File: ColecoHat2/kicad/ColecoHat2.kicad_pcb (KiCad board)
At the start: 2 copper layers, 56 x 65 mm, 20 parts, among them J1 CTRL1, J2 CTRL2, J3 PI_HEADER, J4 CONN_01X06, SW1 BOOTLOADER, SW2 RESET, U1 STM32L011G4U6

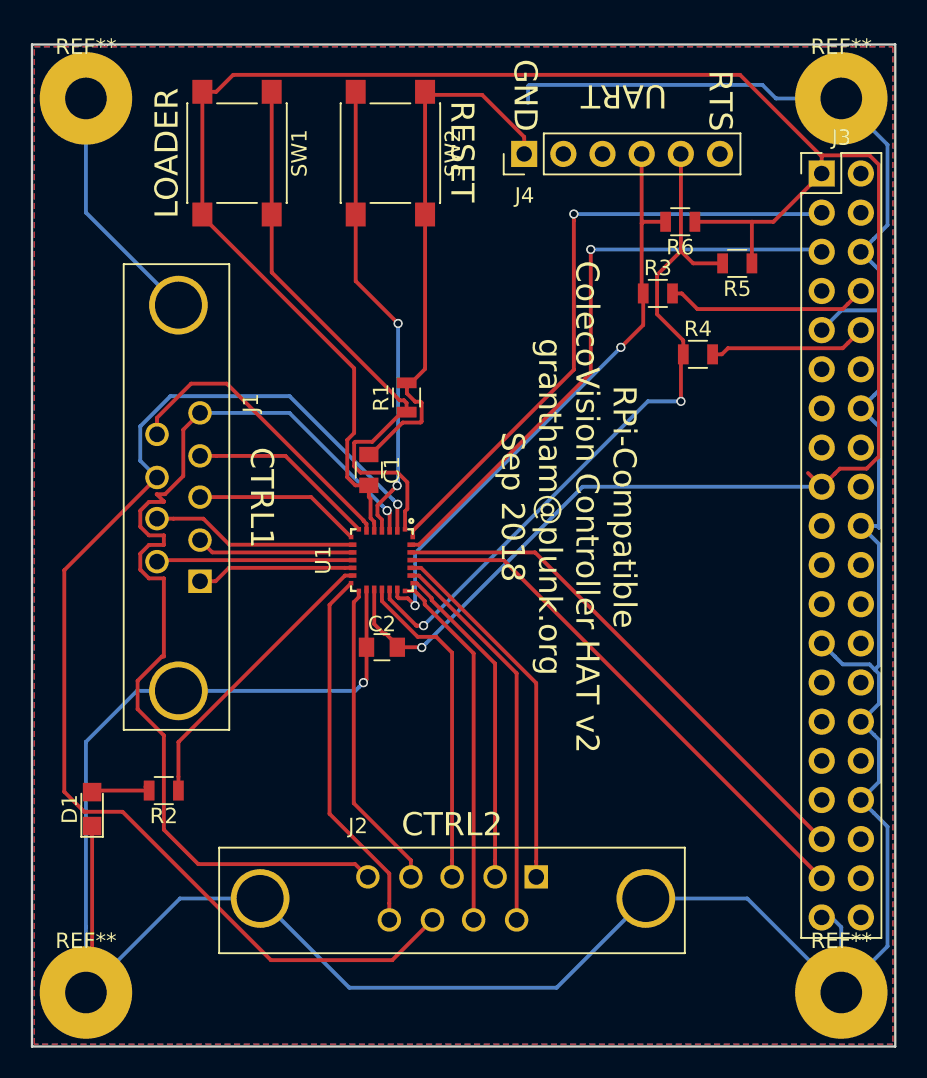
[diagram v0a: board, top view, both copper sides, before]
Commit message: add larger STM32L041K6U6 component
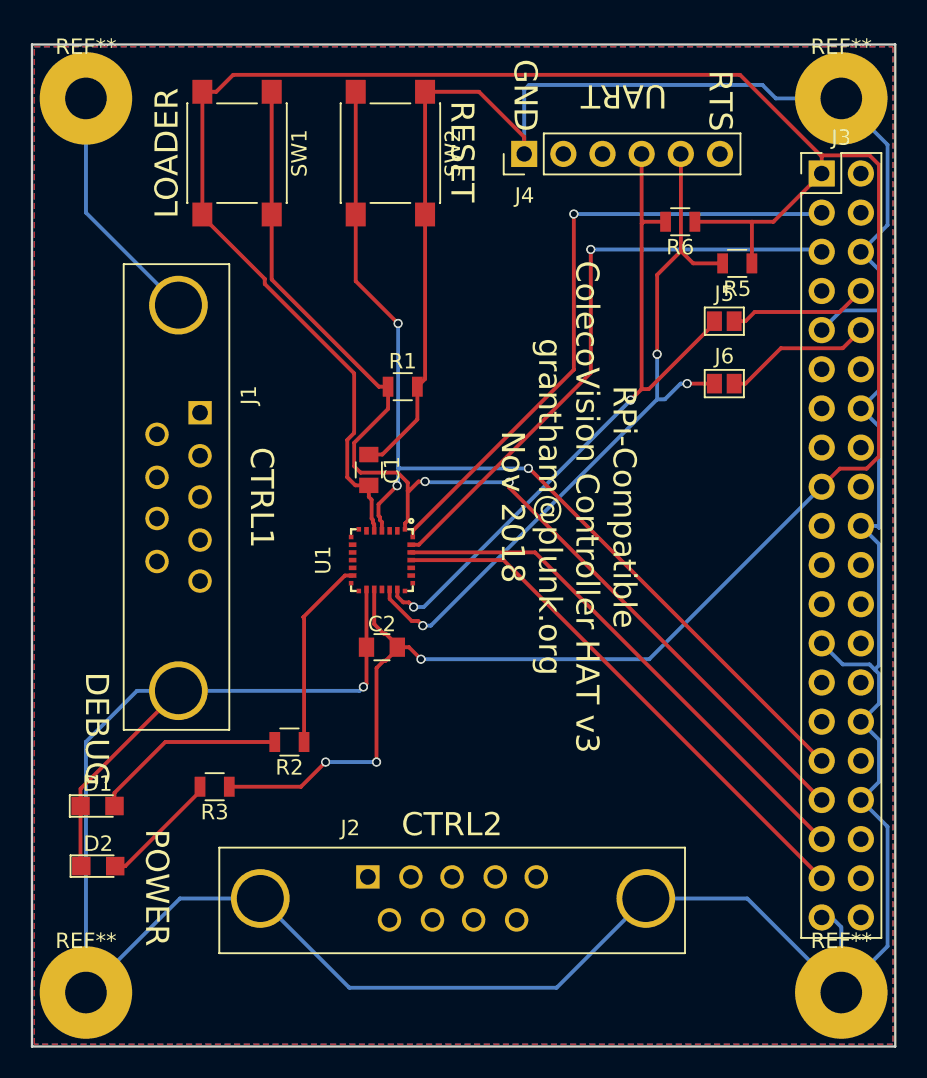
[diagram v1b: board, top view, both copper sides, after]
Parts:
- removed R4: 0, Resistors_SMD:R_0805
- added D2: POWER, LEDs:LED_0805, F.Cu at (131.8, 109.8)
- added J5: GS2, Connectors:GS2, F.Cu at (172.4, 74.5)
- added J6: GS2, Connectors:GS2, F.Cu at (172.4, 78.5)
- D1: value DEBUG LED -> DEBUG
- J1, J2: footprint Connectors:DB9FD -> Connectors:DB9MD
- R2: value 220 -> 470
- R3: value 0 -> 1K
- moved R3 43.0 mm to (139.3, 104.7), turned to 180 degrees
- moved J1 10.9 mm to (138.4, 80.4)
- moved J2 10.9 mm to (149.3, 110.5)
- moved R2 8.74 mm to (144.2, 101.8)
- moved R1 0.74 mm to (151.6, 78.7), turned to 0 degrees
- moved D1 0.40 mm to (131.8, 105.9), turned to 0 degrees
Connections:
- J3 pad 31: Net-(J3-Pad31) -> NRST
- J3 pad 33: Net-(J3-Pad33) -> BOOTLOADER
- R3 pad 1: USART1_RX -> +3V3
- R3 pad 2: Net-(J3-Pad8) -> Net-(D2-Pad2)
- SW2 pad 2: Net-(SW2-Pad2) -> NRST
- U1 pad 10: S1 -> W1
- U1 pad 11: FIRE1 -> E1
- U1 pad 12: N1 -> QUADB1
- U1 pad 14: QUADB2 -> N2
- U1 pad 15: E2 -> FIRE2
- U1 pad 18: W2 -> S2
- U1 pad 22: S2 -> W2
- U1 pad 23: FIRE2 -> E2
- U1 pad 24: N2 -> QUADB2
- U1 pad 4: Net-(SW2-Pad2) -> NRST
- U1 pad 6: QUADB1 -> N1
- U1 pad 7: E1 -> FIRE1
- U1 pad 8: W1 -> S1
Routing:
- net SELECT_JOYSTICK: track 78.3 -> 0.00 mm, vias 1 -> 0
- net SELECT_KEYPAD: track 65.6 -> 0.00 mm, vias 1 -> 0
- net NRST: track 0.00 -> 65.4 mm, vias 0 -> 3
- net GND: track 266.1 -> 301.5 mm
- net BOOTLOADER: track 37.3 -> 71.5 mm, vias 0 -> 2
- net Net-(SW2-Pad2): track 30.1 -> 0.00 mm, vias 2 -> 0
- net DEBUG_GPIO: track 35.2 -> 5.99 mm
- net FIRE2: track 25.5 -> 0.00 mm
- net QUADB2: track 24.0 -> 0.00 mm
- net N2: track 23.8 -> 0.00 mm
- net QUADA2: track 23.5 -> 0.00 mm
- net S2: track 21.4 -> 0.00 mm
- net W2: track 21.2 -> 0.00 mm
- net E2: track 20.2 -> 0.00 mm
- net QUADB1: track 19.8 -> 0.00 mm
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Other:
- board text added: "DEBUG"
- board text added: "POWER"
- board text added: "RPi-Compatible ColecoVision Controller HAT v3 grantham@plunk.org Nov 2018"
- board text removed: "RPi-Compatible ColecoVision Controller HAT v2 grantham@plunk.org Sep 2018"
